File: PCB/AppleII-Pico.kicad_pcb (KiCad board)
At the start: 2 copper layers, 106.3 x 56.7 mm, 29 parts, among them J1 Apple II, J2 DB15_Female_HighDensity_Mount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, J3 NOPAL, J4 Conn_02x08_Odd_Even, U1 74LCX16245, U2 74LCX16245, U5 PALCE16V8H, U6 Pi PICO, U7 AZ1117

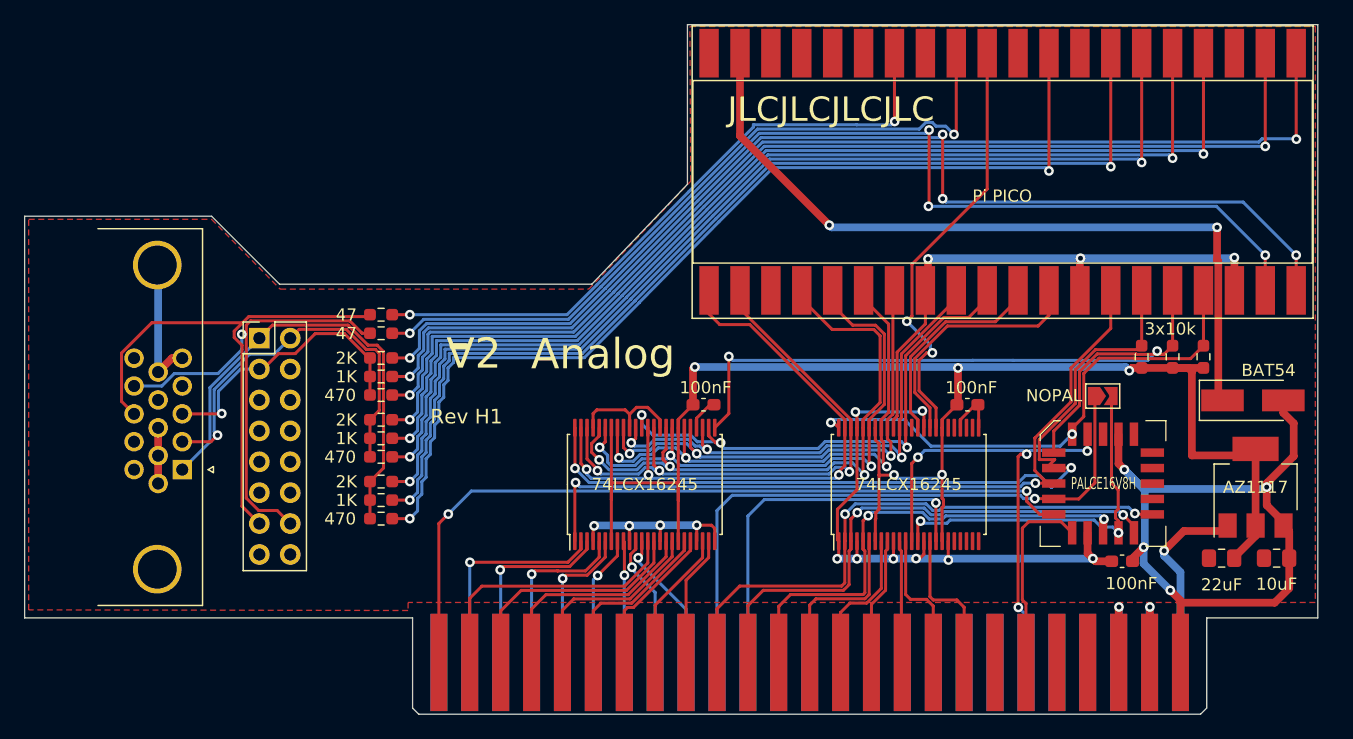
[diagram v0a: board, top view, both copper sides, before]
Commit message: Better RPi Pico footprint
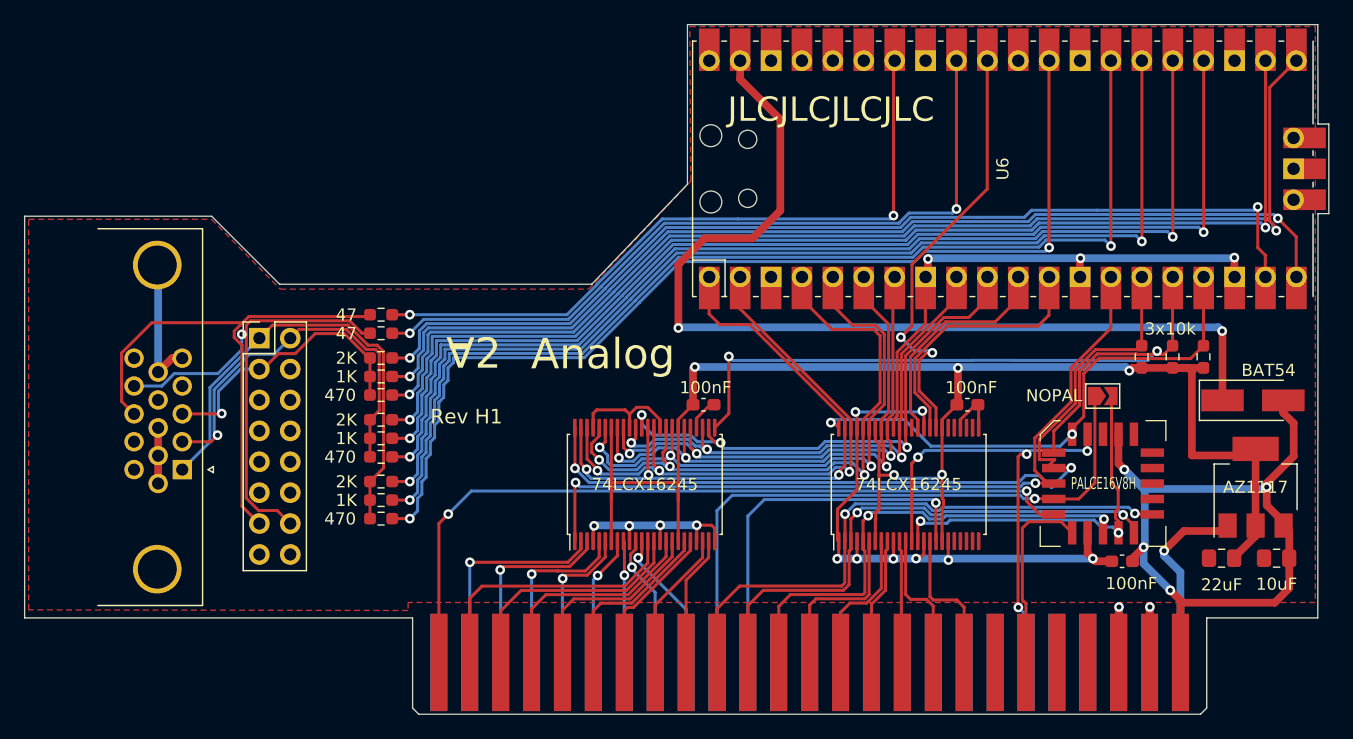
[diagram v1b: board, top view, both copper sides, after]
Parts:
- U6: footprint Package_DIP:DIP-40_W16.51mm_SMDSocket_LongPads -> MCU_RaspberryPi_and_Boards:RPi_Pico_SMD_TH
- moved U6 2.24 mm to (158.0, 89.7)
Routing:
- net Net-(D1-Pad1): track 63.5 -> 79.7 mm
- net B1: track 94.1 -> 86.5 mm, vias 4 -> 2
- net B2: track 91.3 -> 84.3 mm, vias 4 -> 2
- net B0: track 92.2 -> 96.9 mm
- net R1: track 85.2 -> 89.2 mm
- net Net-(R10-Pad1): track 53.7 -> 57.4 mm
- net G2: track 91.7 -> 95.3 mm
- net R0: track 81.4 -> 84.9 mm
- net R2: track 86.4 -> 89.7 mm
- net G0: track 87.1 -> 90.4 mm
- net G1: track 88.3 -> 91.6 mm
- net Net-(R11-Pad1): track 60.6 -> 62.8 mm
- net LPHI0: track 35.7 -> 36.9 mm
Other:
- board size 106.3 x 56.7 mm -> 107.2 x 56.7 mm
- board text added: "Apple II VGA PicoPal"
- board text added: "Board redesign by Hans Hübner https://github.com/hanshuebner/AppleII-VGA Original Board Design by David Kuder Copyright © 2022 https://github.com/dkgrizzly/AppleII-VGA Based on Apple II VGA by Mark Aikens https://github.com/markadev/AppleII-VGA"
- board text removed: "Apple II VGA Board redesign by Hans Hübner"
- board text removed: "Original Board Design by David Kuder Copyright © 2022 https://github.com/dkgrizzly/AppleII-VGA Based on Apple II VGA by Mark Aikens https://github.com/markadev/AppleII-VGA"
- board text removed: "https://github.com/hanshuebner/AppleII-VGA"
